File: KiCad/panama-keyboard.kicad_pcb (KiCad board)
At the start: 2 copper layers, 304.8 x 124.6 mm, 172 parts, among them J1 MX, J2 USB_C_Receptacle_USB2.0, J3 AVR-ISP-6, K1 MX, M1 MX, P1 MX, Q1 MX, T1 MX, U1 MX, U2 ATmega32A-PU, X1 MX, Y1 MX, Y2 Crystal

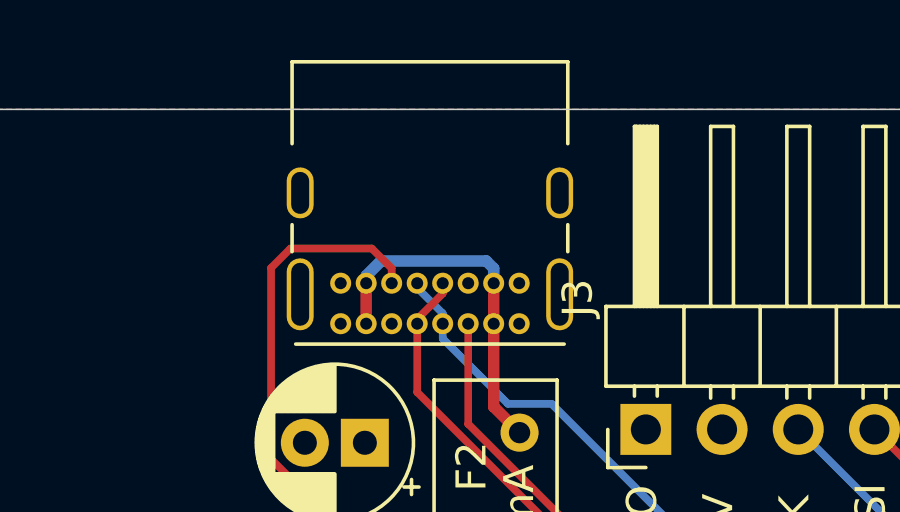
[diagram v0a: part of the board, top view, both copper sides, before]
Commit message: added usb c connector model
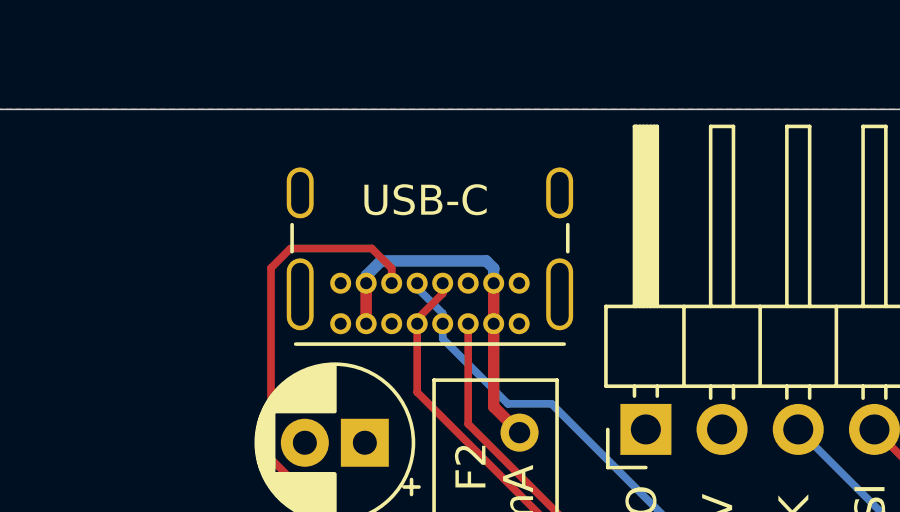
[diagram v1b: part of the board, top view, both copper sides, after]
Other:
- board text added: "USB-C"
